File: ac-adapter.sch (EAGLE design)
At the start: 88 parts, among them IC1 SSC3S900, IC2 TL431, Q1 300V 5A, Q2 300V 5A, Q3 TLP621-1, T1 COMMON_FILTER-SU10VFC, T2 TRANSFORMAER_FLYBACK-ETD34

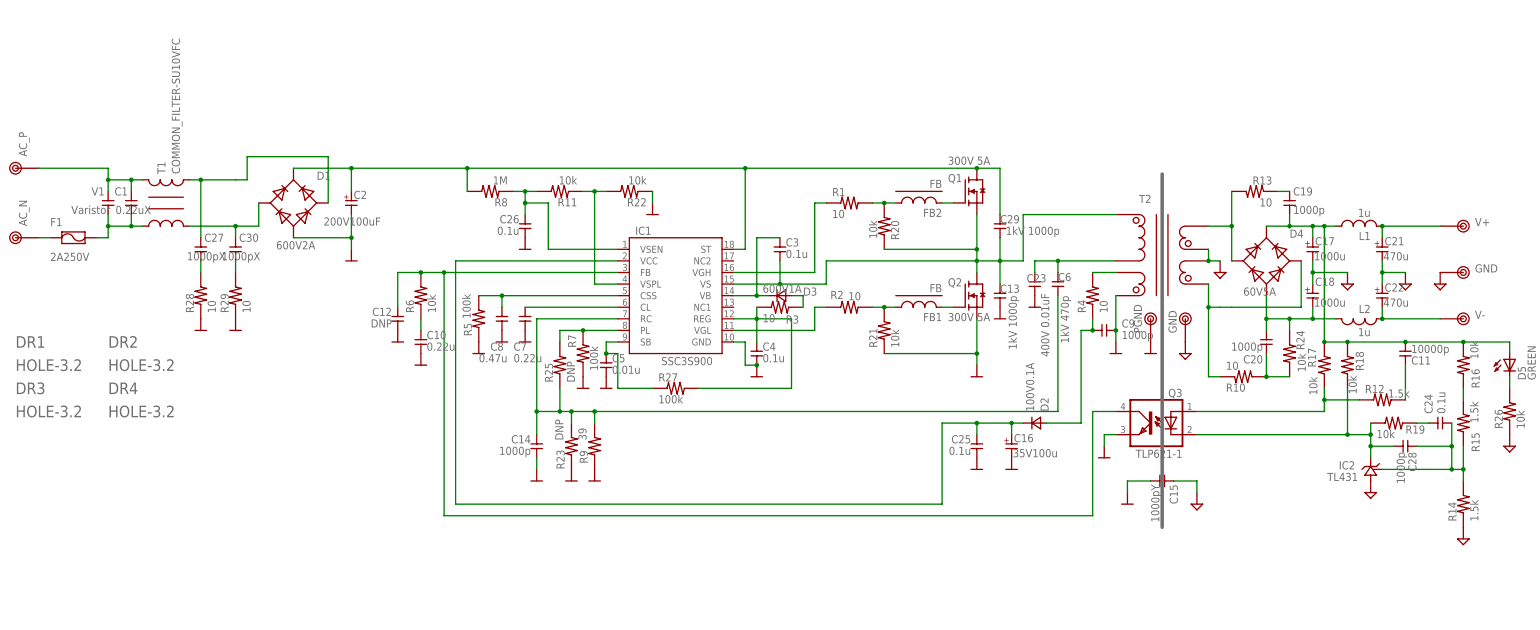
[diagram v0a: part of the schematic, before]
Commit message: UCC256404Aに変更
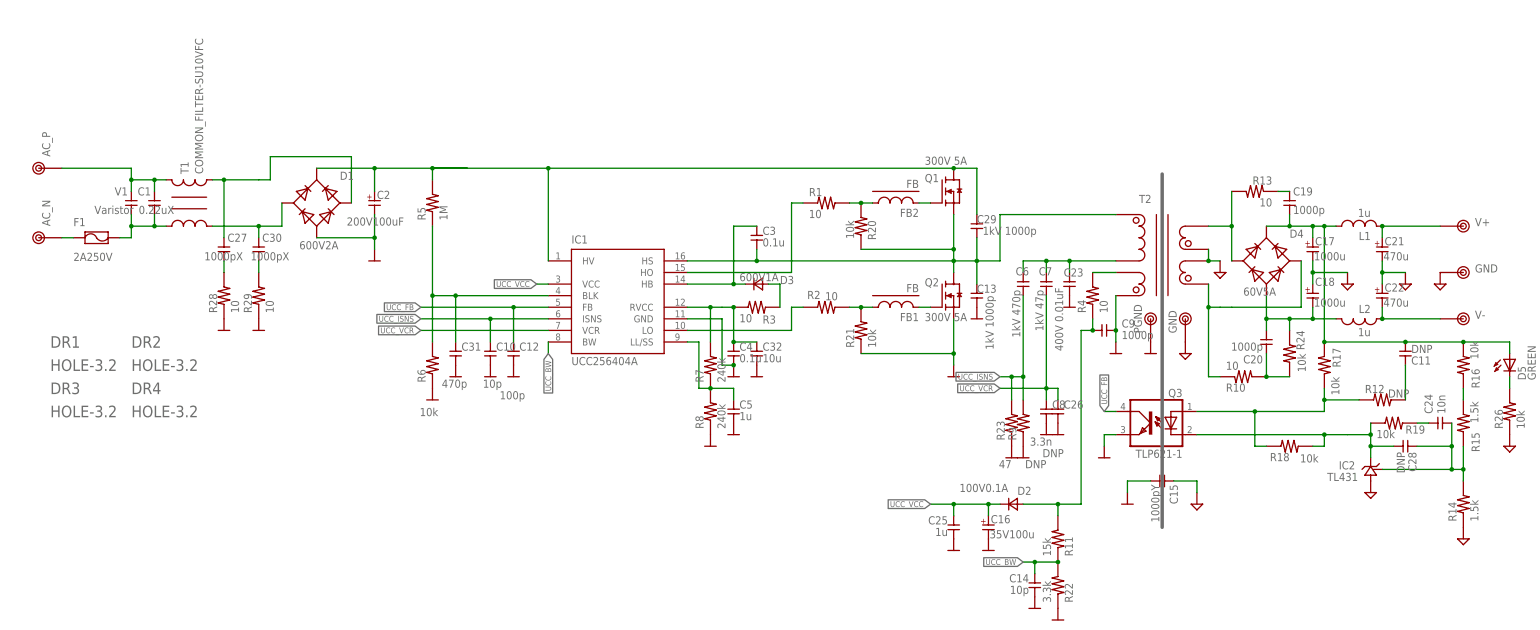
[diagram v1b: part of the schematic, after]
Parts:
- removed R25: DNP, my_rcl:R-1608
- removed R27: 100k, my_rcl:R-1608
- added C31: 470p, my_rcl:C-1608
- added C32: 10u, my_rcl:C-2012
- C10: value 0.22u -> 10p
- C11: value 10000p -> DNP
- C12: value DNP -> 100p
- C14: value 1000p -> 10p
- C24: value 0.1u -> 10n
- C25: value 0.1u -> 1u
- C26: value 0.1u -> DNP
- C28: value 1000p -> DNP
- C5: value 0.01u -> 1u
- C6: device my_rcl:C-5 -> my_rcl:C-3225
- C7: value 0.22u -> 1kV 47p; device my_rcl:C-1608 -> my_rcl:C-3225
- C8: value 0.47u -> 3.3n
- IC1: value SSC3S900 -> UCC256404A; device my_ic:SSC3S900 -> my_ic:UCC25640X
- R11: value 10k -> 15k
- R12: value 1.5k -> DNP
- R22: value 10k -> 3.3k
- R23: value DNP -> 47
- R5: value 100k -> 1M; device my_rcl:R-1608 -> my_rcl:R-10
- R7: value 100k -> 240k
- R8: value 1M -> 240k; device my_rcl:R-7.5 -> my_rcl:R-1608
- R9: value 39 -> DNP
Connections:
- net VCC renamed UCC_VCC
- removed net N$19: C7.1, IC1.CL
- removed net N$20: C8.1, IC1.CSS, R5.2
- removed net N$21: C10.1, R6.1
- removed net N$25: C12.1, IC1.FB, Q3.COL, R6.2
- removed net N$27: C14.1, C6.2, IC1.RC, R23.2, R25.1, R9.2
- removed net N$28: IC1.VSPL, R11.1, R22.2
- removed net N$31: C26.1, IC1.VSEN, R11.2, R8.1
- new net UCC_BW: C14.1, IC1.BW, R11.1, R22.2
- new net UCC_FB: C12.1, IC1.FB, Q3.COL
- new net UCC_ISNS: C10.1, C6.2, IC1.ISNS, R23.2, R9.2
- new net UCC_VCR: C26.1, C7.2, C8.1, IC1.VCR
- net N$12: now also IC1.LO; no longer IC1.VGL
- net N$13: now also IC1.HO; no longer IC1.VGH
- net N$14: now also IC1.HB; no longer IC1.VB
- net N$16: now also C32.1, IC1.RVCC, R7.2; no longer IC1.REG, R27.2
- net N$17: now also IC1.LL/SS, R7.1, R8.2; no longer IC1.SB, R27.1
- net N$18: now also C31.1, IC1.BLK, R5.1, R6.2; no longer IC1.PL, R25.2, R7.2
- net N$24: now also R11.2
- net N$34: now also R18.2
- net N$40: no longer R18.2
- net N$8: now also C7.1
- net PGND: now also C31.2, C32.2, R6.1, R8.1; no longer C7.2, R5.1, R7.1
- net SW: now also IC1.HS; no longer IC1.VS
- net VH: now also IC1.HV, R5.2; no longer IC1.ST, R8.2
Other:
- moved on the sheet: C1, C10, C12, C13, C14, C16, C2, C23, C25, C26, C27, C29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

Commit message: GaN
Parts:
- added D6, D7: SBD, my_rcl:SBD-1A2
- Q1, Q2: device my_ic:NMOS-DFN -> my_ic:NMOS-GAN
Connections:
- net PGND: now also D7.A
- net SW: now also D6.A, D7.K
- net VH: now also D6.K
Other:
- moved on the sheet: C1, C10, C12, C2, C27, C3, C30, C31, C32, C4, C5, D1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

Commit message: 値修正
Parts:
- C6: value 1kV 470p -> 220p 1kV
- C7: value 1kV 47p -> 100p 1kV
- C8: value 3.3n -> 6.8n
- R1, R2: value 10 -> 120
- R17, R18: value 10k -> 1.5k
- R23: value 47 -> 120

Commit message: ver2.3 GaNとSiを共通に
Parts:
- removed D6, D7: SBD, my_rcl:SBD-1A2
- removed Q2: 300V 5A, my_ic:NMOS-GAN
- added C33, C34, C35, C36, C37, C38: 10u, my_rcl:C-3225-2
- added R25: 240k, my_rcl:R-1608
- C12: value 100p -> 22p
- C2: device my_rcl:CPOLE7.5-16A2 -> my_rcl:CPOLE7.5-16A3
- D3: device my_rcl:DIODE-7 -> my_rcl:DIODE-1N4148W
- Q1: value 300V 5A -> 200V 3A; device my_ic:NMOS-GAN -> my_ic:NMOS_FET_HALF
- R3: value 10 -> 39; device my_rcl:R-2012 -> my_rcl:R-1608
- R5: value 1M -> 240k; device my_rcl:R-10 -> my_rcl:R-1608
- R6: value 10k -> 6.8k
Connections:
- removed net N$39: FB1.2, Q2.G
- removed net N$41: FB2.2, Q1.G
- new net N$13: C13.1, FB1.2
- new net N$19: C29.2, FB2.1
- new net N$21: R25.2, R5.1
- net GND: now also C33.2, C34.1, C35.2, C36.1, C37.2, C38.1
- net N$14: now also R3.1; no longer D3.K
- net N$15: now also D3.K; no longer D3.A
- net N$16: now also D3.A; no longer R3.1
- net N$18: now also R25.1; no longer R5.1
- net N$2: now also Q1.GT; no longer FB2.1
- net N$40: now also C33.1, C37.1
- net N$7: now also C34.2, C38.2
- net N$9: now also Q1.GB; no longer FB1.1
- net PGND: now also Q1.V-; no longer D7.A, Q2.S
- net SW: now also FB1.1, FB2.2, Q1.SW; no longer C13.1, C29.2, D6.A, D7.K, Q1.S, Q2.D
- net V+: now also C35.1
- net V-: now also C36.2
- net VH: now also Q1.V+; no longer D6.K, Q1.D
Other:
- moved on the sheet: C13, C17, C18, C21, C22, C29, D3, FB1, FB2, L1, L2, R2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

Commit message: 曲げる前
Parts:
- removed FB2: FB, my_rcl:FB-1608FB
- added C39: DNP, my_rcl:C-1608
- added FB3: FB-3216, my_rcl:FB-3216
- added R27: Thermistor, my_rcl:THERMISTOR
- C37, C38: value 10u -> 1u; device my_rcl:C-3225-2 -> my_rcl:C-2012-2
- FB1: value FB -> FB-1608FB
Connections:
- removed net N$19: C29.2, FB2.1
- new net N$25: D1.V+, R27.1
- new net N$27: FB3.2, T2.L1_P
- net N$13: now also C29.1; no longer C13.1
- net N$40: now also C39.2
- net N$6: now also C39.1
- net PGND: now also C29.2
- net SW: now also C13.1, FB3.1; no longer FB1.1, FB2.2, T2.L1_P
- net VH: now also FB1.1, R27.2; no longer C29.1, D1.V+
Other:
- moved on the sheet: C1, C13, C27, C29, C30, D1, D5, F1, FB1, R26, R28, R29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

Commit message: 曲げた
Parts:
- removed TP6: GND, my_connector:TESTPIN-LARGE
- removed TP7: PGND, my_connector:TESTPIN-LARGE
- removed V1: Varistor, my_rcl:C-5
- added C40, C41, C42: 10u, my_rcl:C-3225-2
- added FB2: FB-3216, my_rcl:FB-3216
- added T3: TRANSFORMAER_FLYBACK-ETD34, my_rcl:TRANSFORMAER_FLYBACK-ETD34
- C1: value 0.22uX -> Varistor; device my_rcl:C-X -> my_rcl:C-5
- C10: value 10p -> 1u
- C11: value DNP -> 0.1u
- C12: value 22p -> 10u; device my_rcl:C-1608 -> my_rcl:C-2012
- C13: value 1kV 1000p -> 1u; device my_rcl:C-3225 -> my_rcl:C-1608
- C14: value 10p -> 1kV 1000p; device my_rcl:C-1608 -> my_rcl:C-3225
- C15: value 1000pY -> 1kV 1000p; device my_rcl:C-Y -> my_rcl:C-3225
- C17: value 1000u -> 220p 1kV; device my_rcl:CPOLE5-13 -> my_rcl:C-3225
- C18: value 1000u -> 10p; device my_rcl:CPOLE5-13 -> my_rcl:C-1608
- C19: value 1000p -> 100p 1kV; device my_rcl:C-1608 -> my_rcl:C-3225
- C2: value 200V100uF -> 0.22uX; device my_rcl:CPOLE7.5-16A3 -> my_rcl:C-X
- C20: value 1000p -> 6.8n
- C21: value 470u -> DNP; device my_rcl:CPOLE5-10 -> my_rcl:C-1608
- C22: value 470u -> 450V 0.047uF; device my_rcl:CPOLE5-10 -> my_rcl:C-12.5
- C23: value 400V 0.01uF -> 1000p; device my_rcl:C-12.5 -> my_rcl:C-1608
- C24: value 10n -> 1000pY; device my_rcl:C-1608 -> my_rcl:C-Y
- C25: value 1u -> 470p
- C26: value DNP -> 470p
- C27: value 1000pX -> 1u; device my_rcl:C-5 -> my_rcl:C-2012-2
- C28: value DNP -> 1u; device my_rcl:C-1608 -> my_rcl:C-2012-2
- C29: value 1kV 1000p -> 1000u; device my_rcl:C-3225 -> my_rcl:CPOLE5-13
- C3, C4: value 0.1u -> 1000pX; device my_rcl:C-1608 -> my_rcl:C-3216
- C30: value 1000pX -> 1000u; device my_rcl:C-5 -> my_rcl:CPOLE5-13
- C31: value 470p -> DNP
- C32: value 10u -> DNP; device my_rcl:C-2012 -> my_rcl:C-1608
- C35: value 10u -> 10n; device my_rcl:C-3225-2 -> my_rcl:C-1608
- C36: value 10u -> 470u; device my_rcl:C-3225-2 -> my_rcl:CPOLE5-10
- C37: value 1u -> 470u; device my_rcl:C-2012-2 -> my_rcl:CPOLE5-10
- C38: value 1u -> DNP; device my_rcl:C-2012-2 -> my_rcl:C-1608
- C39: value DNP -> 10u; device my_rcl:C-1608 -> my_rcl:C-3225-2
- C5: value 1u -> 200V220uF; device my_rcl:C-1608 -> my_rcl:CPOLE7.5-16A3
- C6: value 220p 1kV -> 470p; device my_rcl:C-3225 -> my_rcl:C-1608
- C7: value 100p 1kV -> 10p; device my_rcl:C-3225 -> my_rcl:C-1608
- C8: value 6.8n -> 22p
- C9: value 1000p -> 0.1u
- D2: value 100V0.1A -> 600V1A
- D3: value 600V1A -> 100V0.1A
- FB1: value FB-1608FB -> FB2012-FB; device my_rcl:FB-1608FB -> my_rcl:FB2012-FB
- FB3: value FB-3216 -> FB2012-FB; device my_rcl:FB-3216 -> my_rcl:FB2012-FB
- R1, R2: value 120 -> 10
- R10: value 10 -> 120
- R11: value 15k -> 120; device my_rcl:R-1608 -> my_rcl:R-2012
- R12: value DNP -> 10k
- R13, R29: value 10 -> 10k; device my_rcl:R-2012 -> my_rcl:R-1608
- R14: value 1.5k -> 120
- R15: value 1.5k -> DNP
- R16: value 10k -> 22k
- R17: value 1.5k -> 3.3k
- R18: value 1.5k -> 10; device my_rcl:R-1608 -> my_rcl:R-2012
- R19, R20: value 10k -> 10; device my_rcl:R-1608 -> my_rcl:R-2012
- R22: value 3.3k -> 1.5k
- R23: value 120 -> 1.5k
- R24: value 10k -> DNP
- R25: value 240k -> 10k
- R27: value Thermistor -> 1.5k; device my_rcl:THERMISTOR -> my_rcl:R-1608
- R28: value 10 -> 1.5k; device my_rcl:R-2012 -> my_rcl:R-1608
- R3: value 39 -> Thermistor; device my_rcl:R-1608 -> my_rcl:THERMISTOR
- R4: value 10 -> 240k; device my_rcl:R-2012 -> my_rcl:R-1608
- R9: value DNP -> 39
- T1: value COMMON_FILTER-SU10VFC -> COMMON_FILTER-SMALL; device my_rcl:COMMON_FILTER-SU10VFC -> my_rcl:COMMON_FILTER-SMALL
- T2: value TRANSFORMAER_FLYBACK-ETD34 -> COMMON_FILTER-SU10VFC; device my_rcl:TRANSFORMAER_FLYBACK-ETD34 -> my_rcl:COMMON_FILTER-SU10VFC
- renumbered Q3 to Q2
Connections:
- removed net N$40: C11.2, C17.1, C19.2, C33.1, C37.1, C39.2, D4.V+, D5.A, L1.1, R16.2, R17.1
- removed net N$7: C18.2, C20.2, C34.2, C38.2, D4.V-, L2.1, R24.1
- new net N$19: C1.1, C2.1, T1.3, T2.1
- new net N$28: C1.2, C2.2, T1.2, T2.4
- new net N$31: C24.2, FB3.2
- new net V+FIL: C36.1, C39.1, C41.1, L1.2, TP3.1
- new net V-FIL: C37.2, C40.2, C42.2, L2.2, TP4.1
- net GND: now also C24.1, C25.2, C26.2, C27.2, C28.1, C29.2, C30.1, C36.2, C37.1, C39.2, C40.1, C41.2, C42.1, R21.1, R28.1, R29.1, T3.L3_P, T3.L4_N; no longer C15.1, C17.2, C18.1, C21.2, C22.1, C35.2, C36.1, C37.2, C38.1, R14.1, R26.1, T2.L3_P, T2.L4_N, TP6.1
- net N$1: now also T1.4; no longer C1.1, T1.1, V1.1
- net N$10: now also C25.1, R19.2; no longer C20.1, R10.2, R24.2
- net N$11: now also C3.2, R1.2; no longer C27.2, R28.2
- net N$12: now also R11.2; no longer R2.2
- net N$13: now also C14.1; no longer C29.1
- net N$14: now also C11.1, R9.1; no longer C3.1, R3.1
- net N$15: now also D2.K, R9.2; no longer D3.K, R3.2
- net N$16: now also C12.1, C9.1, D2.A; no longer C32.1, C4.1, D3.A
- net N$17: now also C10.1; no longer C5.1
- net N$18: now also C6.1, R5.1; no longer C31.1, R25.1
- net N$2: now also R10.2, R12.1; no longer R1.2, R20.1
- net N$20: now also R10.1; no longer R1.1
- net N$21: now also R4.1, R5.2; no longer R25.2, R5.1
- net N$22: now also R18.2, T3.L2_N; no longer R4.2, T2.L2_N
- net N$23: now also C31.1, R24.2; no longer C11.1, R12.2
- net N$24: now also C23.1, D3.A, R16.2, R18.1; no longer C9.1, D2.A, R11.2, R4.1
- net N$25: now also R3.1; no longer R27.1
- net N$26: now also T1.1; no longer C1.2, T1.4, V1.2
- net N$27: now also FB2.2, T3.L1_P; no longer FB3.2, T2.L1_P
- net N$29: now also C32.2, R22.1, R25.1; no longer C28.2, R18.1, R19.1
- net N$3: now also C26.1, R20.1; no longer C19.1, R13.1
- net N$32: now also C32.1, C35.2, R27.1, R28.2; no longer C24.2, C28.1, R14.2, R15.1
- net N$33: now also C35.1, R25.2; no longer C24.1, R19.2
- net N$34: now also R22.2, R23.2, R24.1; no longer R12.1, R17.2, R18.2
- net N$35: now also R20.2, T3.L3_N; no longer R13.2, T2.L3_N
- net N$36: now also R19.1, T3.L4_P; no longer R10.1, T2.L4_P
- net N$37: now also R29.2; no longer R26.2
- net N$38: now also C4.2, R2.2; no longer C30.2, R29.2
- net N$4: now also C3.1, T2.2; no longer C27.1, T1.2
- net N$5: now also C4.1, T2.3; no longer C30.1, T1.3
- net N$6: now also C38.1, R26.1, R27.2; no longer C39.1, R15.2, R16.1
- net N$8: now also C17.1, C19.1, C22.1, T3.L1_N; no longer C23.1, C6.1, C7.1, T2.L1_N
- net N$9: now also R11.1, R13.2; no longer R2.1, R21.2
- net PGND: now also C18.2, C20.2, C21.2, C22.2, C6.2, C7.2, FB3.1, R1.1, R13.1, R14.1, R15.1, R17.1, R2.1, T3.L2_P; no longer C2.2, C25.2, C26.2, C29.2, C31.2, C32.2, C4.2, R21.1, R22.1, R23.1, R28.1, R29.1, R9.1, T2.L2_P, TP7.1
- net SW: now also C11.2, C15.1, FB2.1, R12.2; no longer C13.1, C3.2, FB3.1, R20.2
- net UCC_BW: now also C18.1, R16.1, R17.2; no longer C14.1, R11.1, R22.2
- net UCC_FB: now also C8.1; no longer C12.1
- net UCC_ISNS: now also C17.2, C7.1, R14.2, R15.2; no longer C10.1, C6.2, R23.2, R9.2
- net UCC_VCC: now also C13.1, D3.K; no longer C25.1, D2.K
- net UCC_VCR: now also C19.2, C20.1, C21.1; no longer C26.1, C7.2, C8.1
- net V+: now also C27.1, C29.1, C31.2, C33.1, C38.2, D4.V+, D5.A, L1.1, R23.1, R26.2; no longer C21.1, C35.1, L1.2, TP3.1
- net V-: now also C28.2, C30.2, C34.2, D4.V-, L2.1, R21.2; no longer C22.2, C36.2, L2.2, TP4.1
- net VH: now also C5.1, R3.2, R4.2; no longer C2.1, R27.2, R5.2
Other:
- moved on the sheet: C1, C10, C11, C12, C13, C14, C15, C19, C20, C23, C24, C25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

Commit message: 発注
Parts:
- added D6, D7: 0.2A, my_rcl:DIODE-1N4148W
- added J1: FBSEL, my_rcl:SJ-3-2012
- added R30, R31: 39, my_rcl:R-1608
- C1: device my_rcl:C-5 -> my_rcl:VARISTOR
- C33, C34, C39, C40: device my_rcl:C-3225-2 -> my_rcl:C-3225-3
- C41, C42: device my_rcl:C-3225-2 -> my_rcl:C-4532-2
- D3: value 100V0.1A -> 100V0.2A
- D5: value GREEN -> POWER
- FB1, FB3: value FB2012-FB -> FB
- FB2: value FB-3216 -> FB
- R10, R11: device my_rcl:R-2012 -> my_rcl:R-1608
- R9: value 39 -> 10
- T2: value COMMON_FILTER-SU10VFC -> COMMON_FILTER-DUAL; device my_rcl:COMMON_FILTER-SU10VFC -> my_rcl:COMMON_FILTER-DUAL
- TP1: value AC_P -> AC_N
- TP2: value AC_N -> AC_P
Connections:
- new net N$39: D6.K, R30.2
- new net N$7: D7.K, R31.2
- new net V+FB: C31.2, C38.2, D5.A, J1.2, R23.1, R26.2
- net N$12: now also R31.1
- net N$2: now also D6.A
- net N$20: now also R30.1
- net N$29: now also R22.2; no longer R22.1
- net N$34: now also R22.1; no longer R22.2
- net N$9: now also D7.A
- net V+: now also J1.1; no longer C31.2, C38.2, D5.A, R23.1, R26.2
- net V+FIL: now also J1.3
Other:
- moved on the sheet: C10, C11, C12, C2, C3, C31, C32, C33, C34, C35, C36, C37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
